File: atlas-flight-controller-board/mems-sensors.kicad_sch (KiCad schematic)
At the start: 5 parts, among them IC1 LPS22HHTR, IC2 LSM6DSV80XTR, U1 LIS2MDL

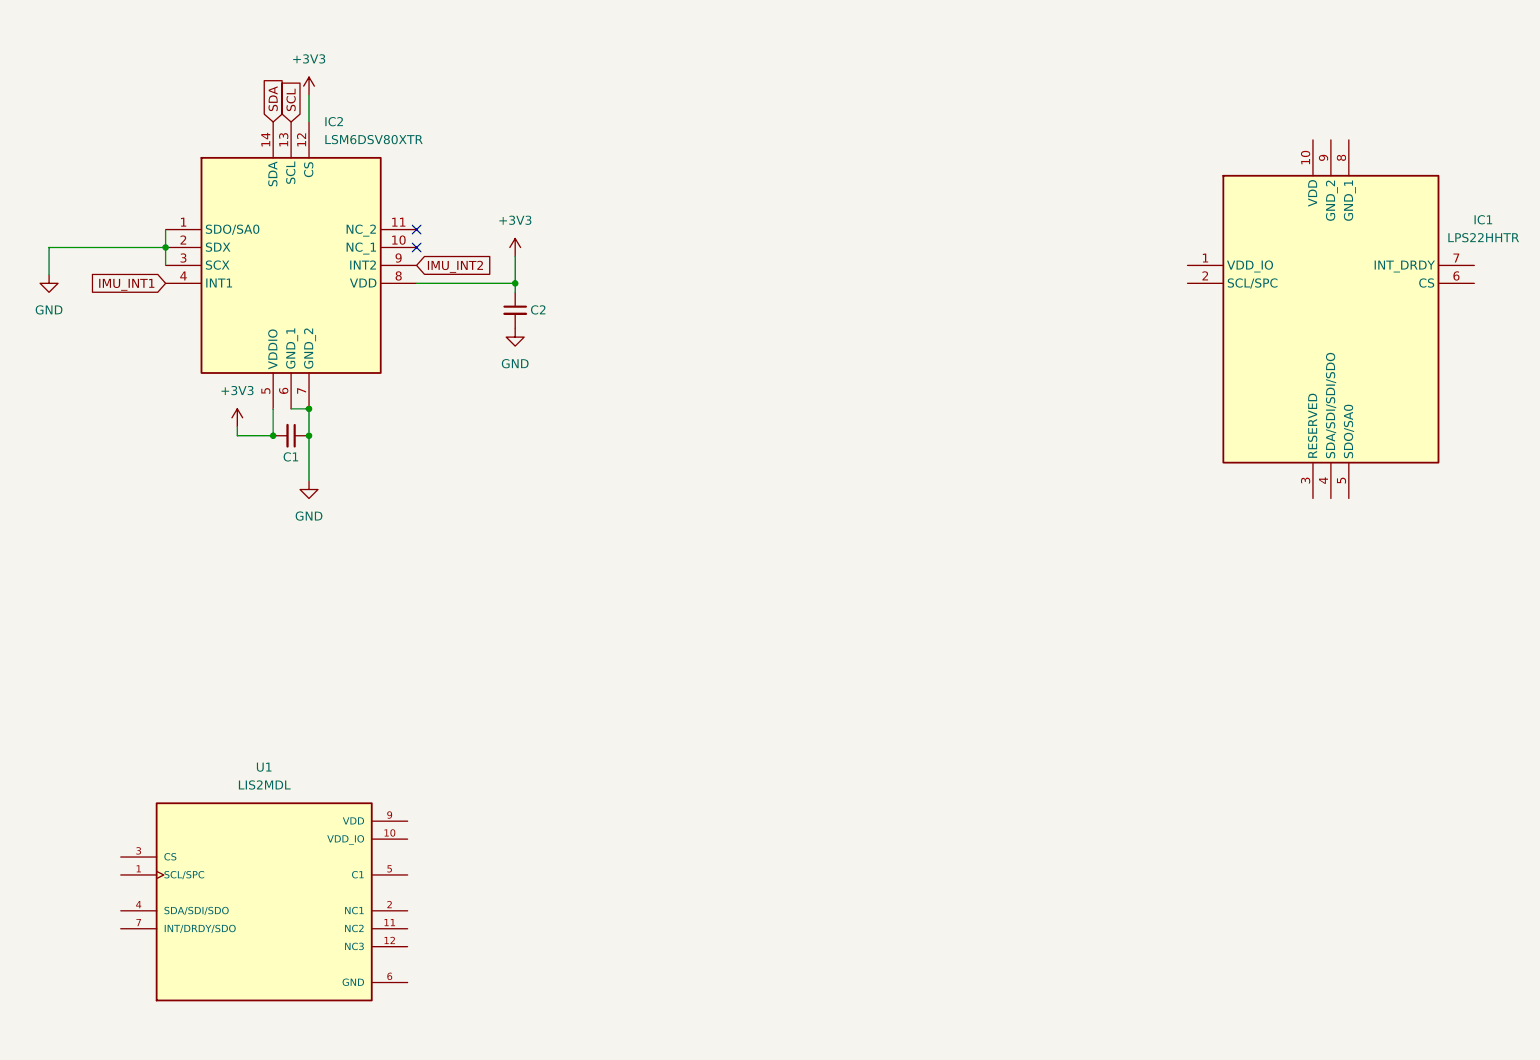
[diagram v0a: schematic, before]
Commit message: Slightly changed default LPS22HH footprint. Finished LPS22HH schematic.
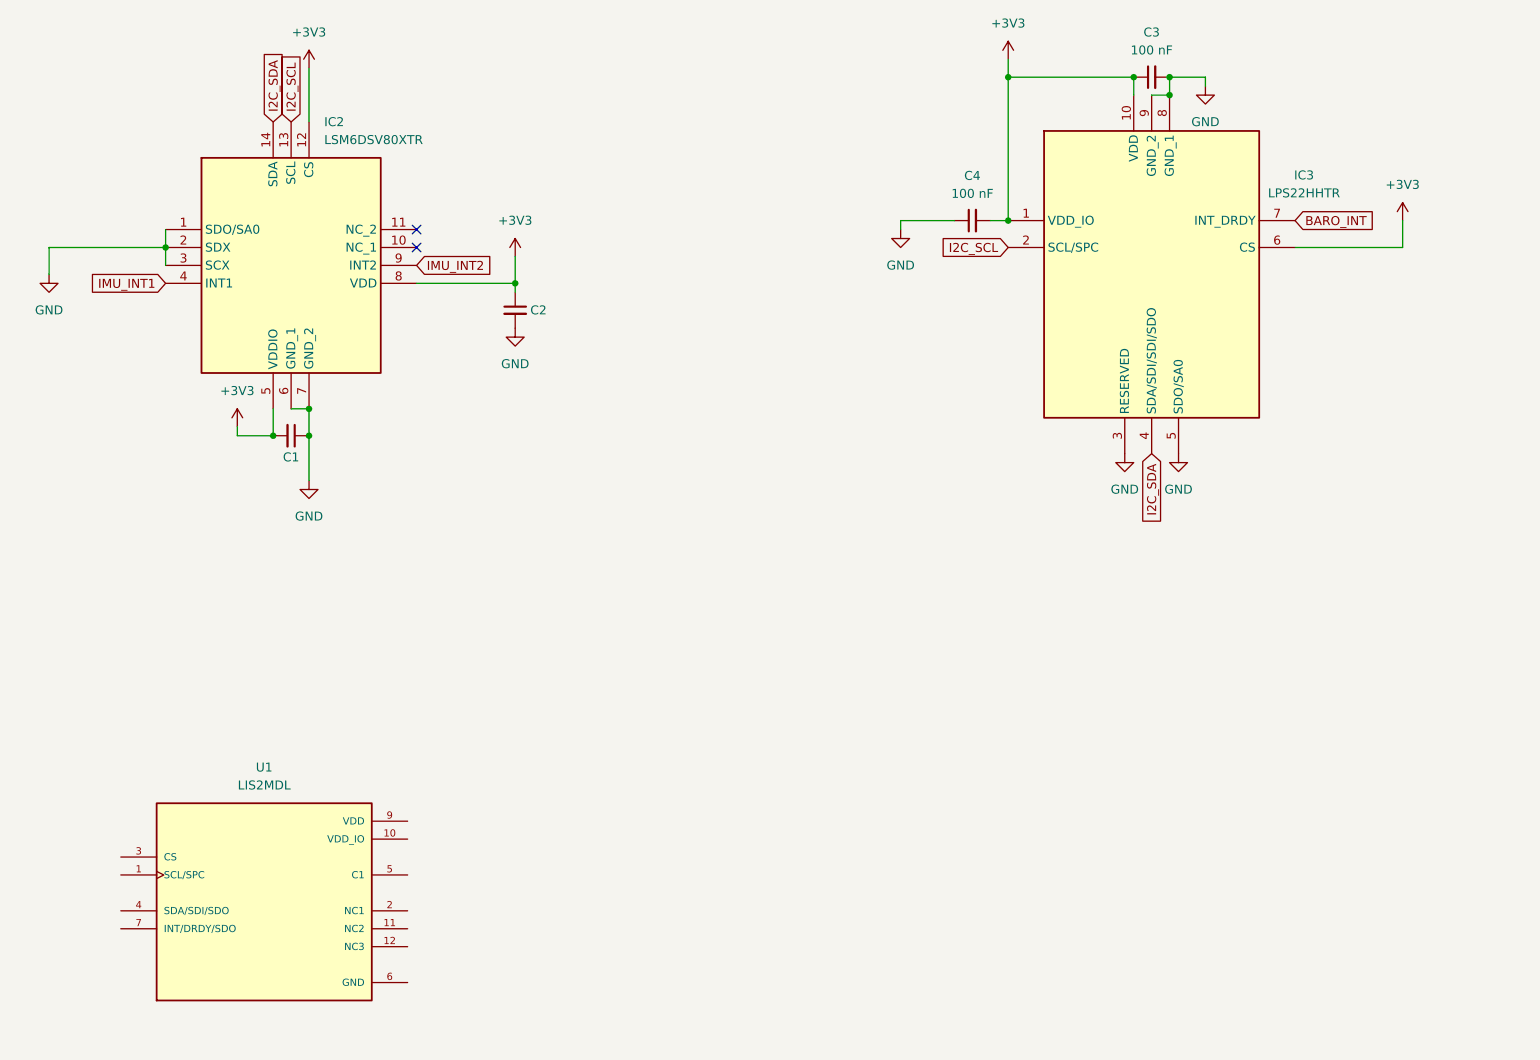
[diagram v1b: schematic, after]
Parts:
- removed IC1: LPS22HHTR, LPS22HHTR:LPS22HHTR, symbol LPS22HHTR:LPS22HHTR
- added C3, C4: 100 nF, Capacitor_SMD:C_0603_1608Metric_Pad1.08x0.95mm_HandSolder, symbol Device:C_Small
- added IC3: LPS22HHTR, LPS22HHTR, symbol LPS22HHTR:LPS22HHTR
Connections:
- net +3V3: now also C3.1, C4.2, IC3.1 (VDD_IO), IC3.10 (VDD), IC3.6 (CS)
- net GND: now also C3.2, C4.1, IC3.3 (RESERVED), IC3.5 (SDO/SA0), IC3.8 (GND_1), IC3.9 (GND_2)
- net SCL renamed I2C_SCL
- net I2C_SCL: now also IC3.2 (SCL/SPC)
- net SDA renamed I2C_SDA
- net I2C_SDA: now also IC3.4 (SDA/SDI/SDI/SDO)
- new net BARO_INT: IC3.7 (INT_DRDY)

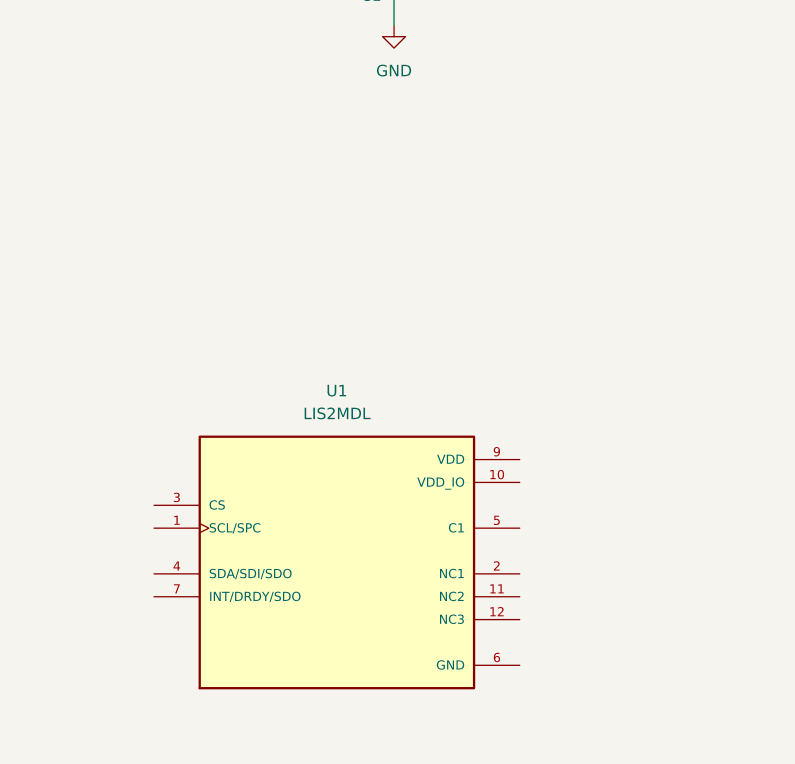
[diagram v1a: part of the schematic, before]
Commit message: Finished Mag Schematic. Modified Alum Poly Cap symbol + footprint.
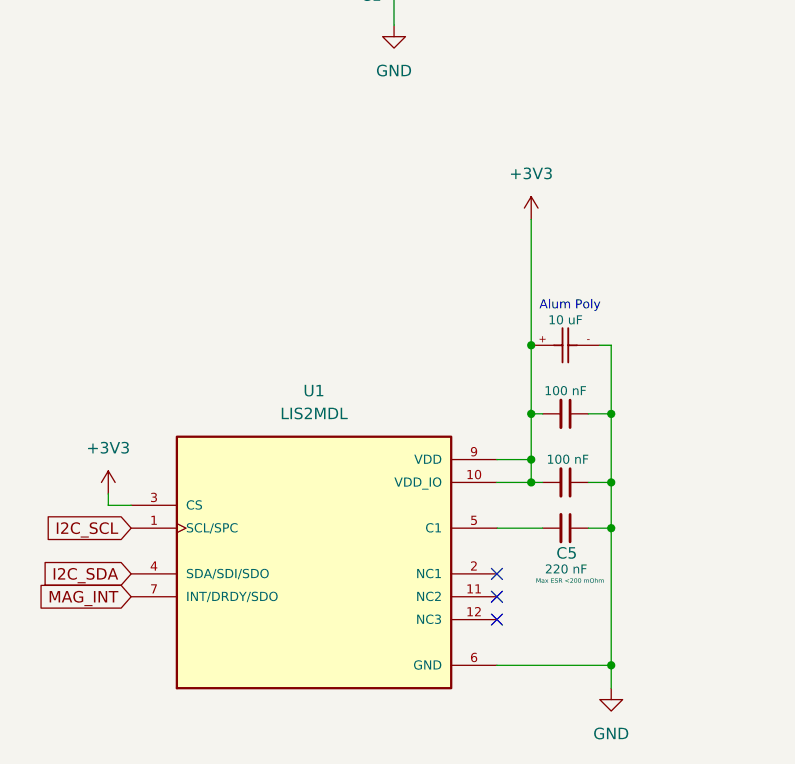
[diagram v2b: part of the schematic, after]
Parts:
- added C5: 220 nF, Capacitor_SMD:C_0603_1608Metric_Pad1.08x0.95mm_HandSolder, symbol Device:C_Small
- added C6: 100 nF, Capacitor_SMD:C_0603_1608Metric_Pad1.08x0.95mm_HandSolder, symbol Device:C_Small
- added C7: 10 uF, CAP_APA_0606_AVX, symbol APA0606100M050R:APA0606100M050R
- added C8: 100 nF, symbol Device:C_Small
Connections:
- net +3V3: now also U1.10 (VDD_IO), U1.3 (CS), U1.9 (VDD), C6.2, C7.+, C8.2
- net GND: now also C5.1, C6.1, C7.-, C8.1
- net I2C_SCL: now also U1.1 (SCL/SPC)
- net I2C_SDA: now also U1.4 (SDA/SDI/SDO)
- net at U1.5 (C1): now also C5.2
- net MAG_INT: now reaches U1.7 (INT/DRDY/SDO)
- no-connect marks 2 -> 5
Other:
- note added: "Alum Poly"
- moved on the sheet: U1

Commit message: Fixed Footprints. Moving onto GPS Next
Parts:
- C7: footprint CAP_APA_0606_AVX -> APA0606100M050R:CAP_APA_0606_AVX
- C8: footprint (none) -> Capacitor_SMD:C_0603_1608Metric_Pad1.08x0.95mm_HandSolder
- IC3: footprint LPS22HHTR -> LPS22HHTR:LPS22HHTR
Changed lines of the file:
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@@
 			)
 		)
-		(property "Footprint" ""
+		(property "Footprint" "Capacitor_SMD:C_0603_1608Metric_Pad1.08x0.95mm_HandSolder"
 			(at 102.87 140.97 0)
 			(effects
@@
 			)
 		)
-		(property "Footprint" "LPS22HHTR"
+		(property "Footprint" "LPS22HHTR:LPS22HHTR"
 			(at 219.71 145.72 0)
 			(effects
@@
 			)
 		)
-		(property "Footprint" "CAP_APA_0606_AVX"
+		(property "Footprint" "APA0606100M050R:CAP_APA_0606_AVX"
 			(at 102.362 126.492 0)
 			(effects

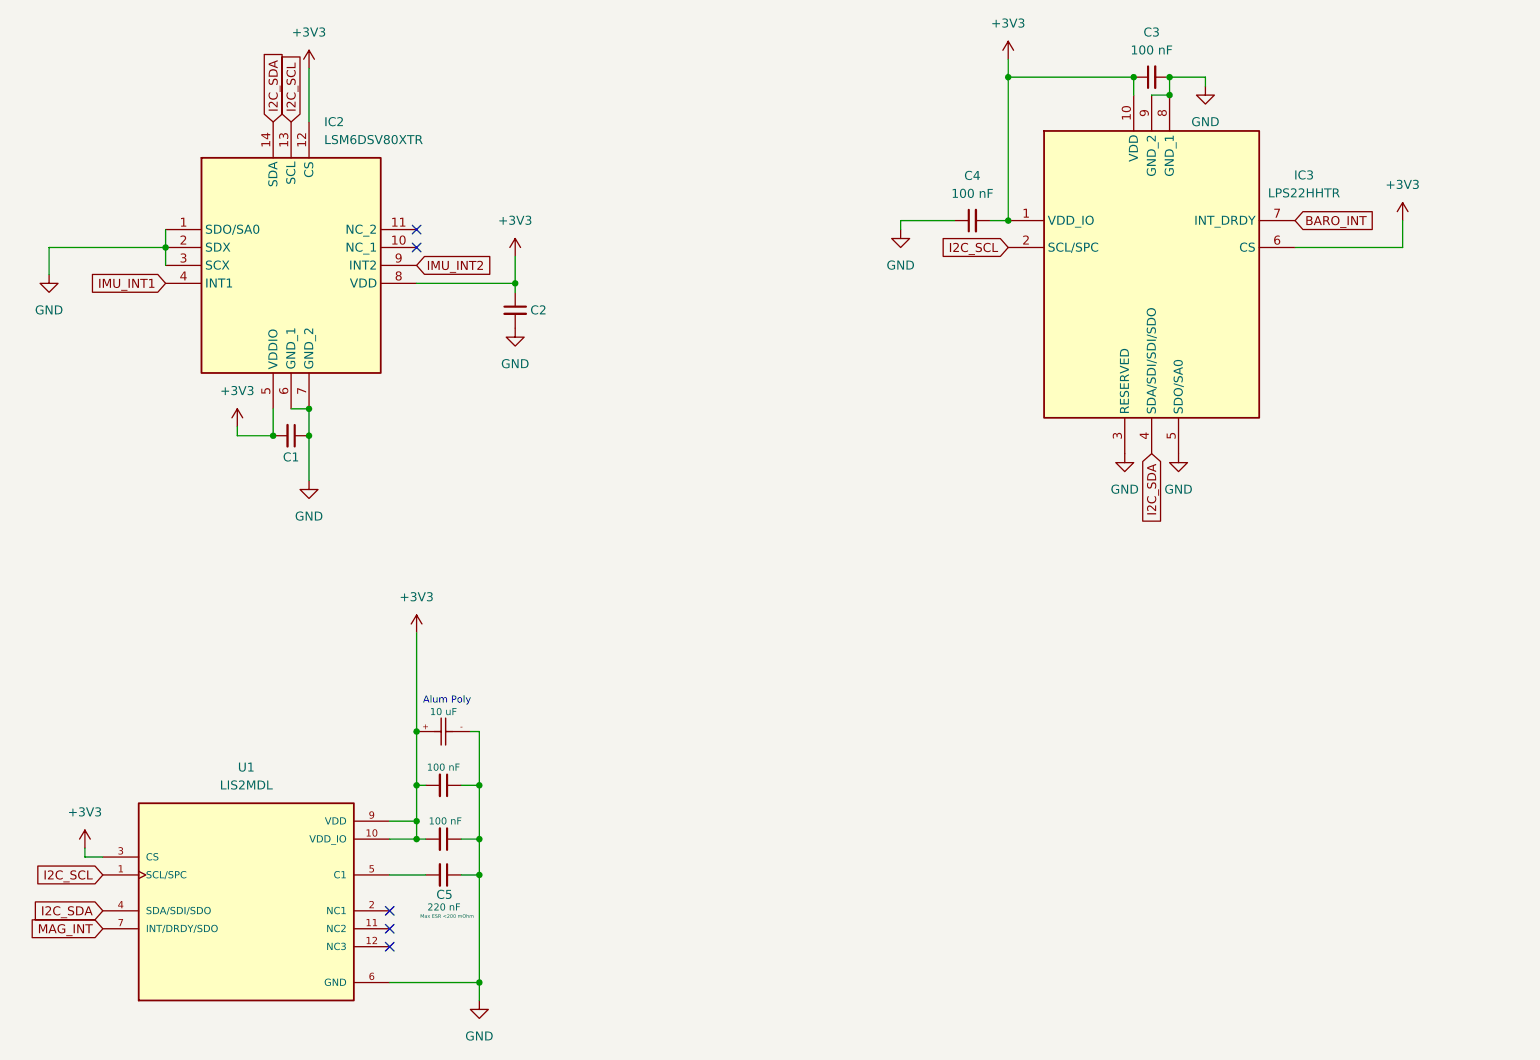
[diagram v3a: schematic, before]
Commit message: wip commit, adding tennsy 4.1 and sd card.
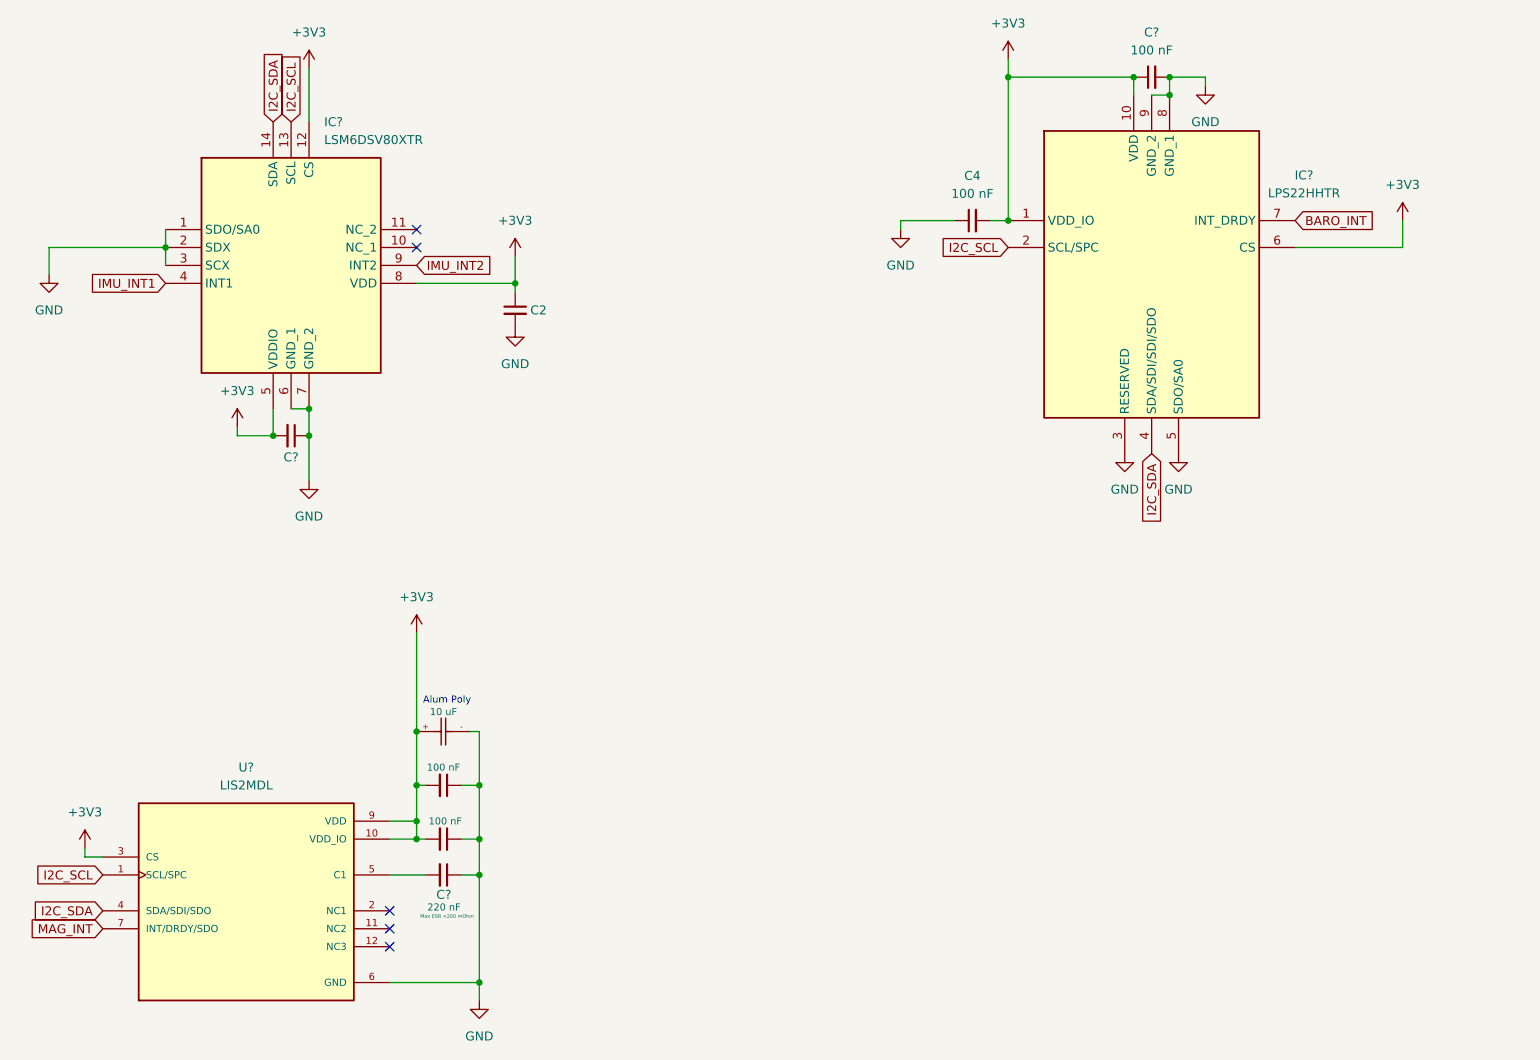
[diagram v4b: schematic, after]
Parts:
- renumbered C8 to C?, C6 to C?, C7 to C?, C3 to C?, C1 to C?, C5 to C?, IC3 to IC?, IC2 to IC?, U1 to U?
